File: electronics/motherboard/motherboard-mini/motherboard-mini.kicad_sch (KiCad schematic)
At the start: 76 parts, among them J1 TBP02R2-381-03BE, J2 TBP02R2-381-02BE, J3 ST1W008S4AR1500, J4 TBP02R2-381-03BE, J5 USB4070-30-C_REVC5, J6 CONUFL001-SMD-T, J7 21992304, J8 Conn_01x04_Male, J9 TBP02R2-381-02BE, Q1 BSS214NW, Q2 AOD417, U1 MCP73832-2-OT, U2 NCP718xSN500, U3 INA219BxD, U4 LT3652IMSE, U6 INA219BxD, U7 LD39015M33R, U8 MIC2145BMM, U9 RFM95W-915S2

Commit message: realign with master branch before kangaroo board is split into seperate repo
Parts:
- removed BT1: 1043, 1043:BAT_1043, symbol 1043:1043
- removed C12, C15: 1uF, Capacitor_SMD:C_0805_2012Metric, symbol Device:C
- removed C13, C16, C18: 10uF, Capacitor_SMD:C_0805_2012Metric, symbol Device:C
- removed C14: 0.01uF, Capacitor_SMD:C_0805_2012Metric, symbol Device:C
- removed C17: 100pF, Capacitor_SMD:C_0805_2012Metric, symbol Device:C
- removed D4: LED, LED_SMD:LED_0805_2012Metric, symbol Device:LED
- removed D5, D6: SS34LW_RVG, SS34LW_RVG:SODFL3718X102N, symbol SS34LW_RVG:SS34LW_RVG
- removed D8: BB-2020BGR-TRB, BB-2020BGR-TRB:LED_BB-2020BGR-TRB, symbol BB-2020BGR-TRB:BB-2020BGR-TRB
- removed D9: D_Schottky, SM5817PL:SODFL3718X108N, symbol Device:D_Schottky
- removed J1, J4: TBP02R2-381-03BE, TBP02R2-381-03BE:CUI_TBP02R2-381-03BE, symbol TBP02R2-381-03BE:TBP02R2-381-03BE
- removed J2, J9: TBP02R2-381-02BE, TBP02R2-381-02BE:CUI_TBP02R2-381-02BE, symbol TBP02R2-381-02BE:TBP02R2-381-02BE
- removed J3: ST1W008S4AR1500, ST1W008S4AR1500:JAE_ST1W008S4AR1500, symbol ST1W008S4AR1500:ST1W008S4AR1500
- removed J6: CONUFL001-SMD-T, CONUFL001-SMD-T:LINX_CONUFL001-SMD-T, symbol CONUFL001-SMD-T:CONUFL001-SMD-T
- removed J7: 21992304, 21992304:TE_21992304, symbol 21992304:21992304
- removed J8: Conn_01x04_Male, Connector_PinHeader_2.54mm:PinHeader_1x04_P2.54mm_Vertical, symbol Connector:Conn_01x04_Male
- removed L1: SRP4020T-5R6M, SRP4020TA-5R6M:IND_SRP4020TA-5R6M, symbol pspice:INDUCTOR
- removed L2: CBC2518T100M, CBC2518T100M:INDC2518X200N, symbol CBC2518T100M:CBC2518T100M
- removed MP1: 9774025151R, 9774025151R:WE_9774025151R, symbol 9774025151R:9774025151R
- removed Q1: BSS214NW, Package_TO_SOT_SMD:SOT-323_SC-70, symbol Transistor_FET:BSS214NW
- removed Q2: AOD417, AOD417:DPAK228P994X240_3N, symbol AOD417:AOD417
- removed R19: 91K, Resistor_SMD:R_0805_2012Metric, symbol Device:R
- removed R20: 330K, Resistor_SMD:R_0805_2012Metric, symbol Device:R
- removed R21: 0.1, Resistor_SMD:R_2512_6332Metric, symbol Device:R
- removed R22: 4.7K, Resistor_SMD:R_0805_2012Metric, symbol Device:R
- removed R28, R31: 100K, Resistor_SMD:R_0805_2012Metric, symbol Device:R
- removed R29: 1M, Resistor_SMD:R_0805_2012Metric, symbol Device:R
- removed R30, R33: 10K, Resistor_SMD:R_0805_2012Metric, symbol Device:R
- removed R34: 1K, Resistor_SMD:R_0805_2012Metric, symbol Device:R
- removed S1: DS04-254-2-02BK-SMT, DS04-254-2-02BK-SMT:SW_DS04-254-2-02BK-SMT, symbol DS04-254-2-02BK-SMT:DS04-254-2-02BK-SMT
- removed S2: RST, PTS636_SM43J_SMTR_LFS:SW_PTS636_SM43J_SMTR_LFS, symbol PTS636_SM43J_SMTR_LFS:PTS636_SM43J_SMTR_LFS
- removed S3: BOOT, PTS636_SM43J_SMTR_LFS:SW_PTS636_SM43J_SMTR_LFS, symbol PTS636_SM43J_SMTR_LFS:PTS636_SM43J_SMTR_LFS
- removed U1: MCP73832-2-OT, Package_TO_SOT_SMD:SOT-23-5, symbol Battery_Management:MCP73832-2-OT
- removed U2: NCP718xSN500, Package_TO_SOT_SMD:SOT-23-5, symbol Regulator_Linear:NCP718xSN500
- removed U3, U6: INA219BxD, Package_SO:SOIC-8_3.9x4.9mm_P1.27mm, symbol Analog_ADC:INA219BxD
- removed U4: LT3652IMSE, Package_SO:MSOP-12-1EP_3x4mm_P0.65mm_EP1.65x2.85mm, symbol Battery_Management:LT3652IMSE
- removed U7: LD39015M33R, Package_TO_SOT_SMD:SOT-23-5, symbol Regulator_Linear:LD39015M33R
- removed U8: MIC2145BMM, MIC2145BMM:MIC2145BMM, symbol MIC2145BMM:MIC2145BMM
- removed U9: RFM95W-915S2, RFM95W-915S2:XCVR_RFM95W-915S2, symbol RF_Module:RFM95W-915S2
- added C10: 22uF, Capacitor_SMD:C_0805_2012Metric, symbol Device:C
- added C7: 0.1uF, Capacitor_SMD:C_0805_2012Metric, symbol Device:C
- added C8: 12pF, Capacitor_SMD:C_0805_2012Metric, symbol Device:C
- added J1: JTAG, Connector_PinHeader_2.54mm:PinHeader_1x04_P2.54mm_Vertical, symbol Connector_Generic:Conn_01x04
- added J12: JTAG, 3221-10-0100-00:CNC_3221-10-0100-00, symbol Connector:Conn_ARM_JTAG_SWD_10
- added LS1: PS1240P02BT, PS1240P02BT:XDCR_PS1240P02BT, symbol PS1240P02BT:PS1240P02BT
- added Q1: MMDT3904, Package_TO_SOT_SMD:SOT-363_SC-70-6, symbol Transistor_BJT:MMDT3904
- added Q2: BC847, Package_TO_SOT_SMD:SOT-23, symbol Transistor_BJT:BC847
- added SW1: BOOT, 1977223-6:1977223-6, symbol 2022-10-04_00-56-22:1977223-6
- added SW2: RESET, 1977223-6:1977223-6, symbol 2022-10-04_00-56-22:1977223-6
- added SW3: PROG_BTN, 1977223-6:1977223-6, symbol 2022-10-04_00-56-22:1977223-6
- added U1: CP2102N-Axx-xQFN28, Package_DFN_QFN:QFN-28-1EP_5x5mm_P0.5mm_EP3.35x3.35mm, symbol Interface_USB:CP2102N-Axx-xQFN28
- added U2: ESP32-WROOM-32E_(16MB), ESP32-WROOM-32E__16MB_:XCVR_ESP32-WROOM-32E_(16MB), symbol ESP32-WROOM-32E__16MB_:ESP32-WROOM-32E_(16MB)
- added Y1: 32.768KHz, ABS07AIG-32:XTAL320X150X90, symbol ABS07AIG-32.768KHZ-T:ABS07AIG-32.768KHZ-T
- C1, C4: value 1uF -> 4.7uF
- C2: value 4.7uF -> 0.1uF
- C3: value 10uF -> 0.1uF
- C5: value 4.7uF -> 1uF
- C6: value 1uF -> 0.1uF
- C9: value 10uF -> 12pF
- D1: value LED(Red) -> LED(Orange)
- D2: value LED(Green) -> LED(Yellow)
- D3: value LED(Red) -> LED(Yellow)
- J5: footprint GCT_USB4070-30-C_REVC5 -> USB4145-03-0230-C_REVA:GCT_USB4145-03-0230-C_REVA
- R1: value 10K -> 1K
- R10: value 27K -> 10M
- R12: value 53.6K -> 10K
- R13: value 4.7K -> 1K
- R15: value 680 -> 4.7K
- R17, R2, R6: value 4.7K -> 10K
- R18: value 180K -> 2K
- R4: value 3.2K -> 1K
- R5: value 0.1 -> 1K; footprint Resistor_SMD:R_2512_6332Metric -> Resistor_SMD:R_0805_2012Metric
- R7, R8: value 4.7K -> 0
- R9: value 23K -> 10K
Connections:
- net +12V is gone; now on net GND: C1.1
- net D1 is gone; now on net +3.3V: R6.1
- net I2C_SDA1 is gone; now on net I2C_SCL: R16.2
- net +3.3V: now also C3.2, C4.2, R1.1, R12.1, R15.1, R4.1, R5.2, C10.2, C7.2, J1.1 (Pin_1), J12.1 (VTref), LS1.2, SW3.3, U1.6 (VDD), U2.2 (3V3); no longer R17.1, R3.1, R6.2
- net GND: now also C2.1, C3.1, C4.1, C5.1, C6.2, D3.1 (K), R17.2, C10.1, C7.1, C8.2, J1.4 (Pin_4), J12.3 (GND), J12.5 (GND), J12.9 (GNDDetect), Q2.2 (E), SW1.3, SW2.3, U1.29 (GND), U1.3 (GND), U2.1 (GND), U2.15 (GND), U2.38 (GND), U2.39_1 (GND), U2.39_2 (GND), U2.39_3 (GND), U2.39_4 (GND), U2.39_5 (GND), U2.39_6 (GND), U2.39_7 (GND), U2.39_8 (GND), U2.39_9 (GND); no longer C1.2, C2.2, C3.2, C4.2, C5.2, R10.2, R2.2, R4.1
- net GPIO0: now also Q1.3 (C2), SW1.1, U2.25 (IO0)
- net GPIO2: now also U2.24 (IO2)
- net GPIO4: now also U2.26 (IO4)
- net I2C_SCL: now also U2.37 (IO23)
- net I2C_SDA: now also R15.2, U2.10 (IO25); no longer R17.2
- net SPI_MISO: now also U2.31 (IO19)
- net SPI_MOSI: now also U2.30 (IO18)
- net SPI_SCK: now also U2.29 (IO5)
- net USB_D+: now also U1.4 (D+)
- net USB_D-: now also U1.5 (D-)
- net VBUS: now also C1.2, C2.2, U1.8 (VBUS); no longer C2.1
- net at D1.2 (A): now also R4.2; no longer R2.1
- net GPIO17: now reaches R9.1
- net GPIO17: now also U2.28 (IO17)
- net ESP_ENABLE: now reaches C6.1
- net ESP_ENABLE: now also C5.2, R6.2, Q1.6 (C1), SW2.1, U2.3 (EN)
- net at D1.1 (K): now also U1.19 (~{TXT}/GPIO.0)
- net at D3.2 (A): now also R18.2; no longer R8.2
- net at R1.2: now also U1.9 (~{RST})
- net at D2.2 (A): now also R5.1; no longer R7.2
- net GPIO13: now reaches R18.1
- net GPIO13: now also J12.4 (SWDCLK/TCK), U2.16 (IO13)
- net at D2.1 (K): now also U1.18 (~{RXT}/GPIO.1)
- removed net +5VP: C4.1, R1.1
- net D0 renamed UART_RTS
- net UART_RTS: now also Q1.1 (E1), U1.24 (~{RTS})
- net I2C_SCL1: no longer names the net of R13.2
- net I2C_SCL1: now also LS1.1, Q2.3 (C)
- net VBAT: no longer names the net of C9.1
- net VBAT: now also R10.2, R7.1, Y1.2; no longer C5.1
- new net: R7.2, U2.8 (IO32)
- new net: R12.2, U2.27 (IO16)
- new net: Q2.1 (B), R9.2
- new net: Q1.5 (B2), R3.1
- new net: C8.1, R10.1, R8.1, Y1.1
- new net: R8.2, U2.9 (IO33)
- new net: Q1.2 (B1), R2.1
- new net: U2.17 (NC), U2.18 (NC), U2.19 (NC), U2.20 (NC), U2.21 (NC), U2.22 (NC)
- new net A2: U2.6 (IO34)
- new net GPIO12: J12.8 (NC/TDI), U2.14 (IO12)
- new net GPIO14: J12.2 (SWDIO/TMS), U2.13 (IO14)
- new net GPIO15: J12.6 (SWO/TDO), U2.23 (IO15)
- new net GPIO21: U2.33 (IO21)
- new net GPIO27: U2.12 (IO27)
- new net GPIO36: U2.4 (SENSOR_VP)
- new net GPIO39: U2.5 (SENSOR_VN)
- new net IO_P2: R17.1, SW3.1
- new net UART_DTR: Q1.4 (E2), R2.2, U1.28 (~{DTR})
- new net UART_RX0: J1.2 (Pin_2), U1.26 (TXD), U2.34 (RXD0)
- new net UART_RX1: U2.11 (IO26)
- new net UART_TX0: J1.3 (Pin_3), U1.25 (RXD), U2.35 (TXD0)
- new net UART_TX1: U2.36 (IO22)
- no-connect marks 30 -> 38
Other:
- added sheet cat_m1 (cat_m1.kicad_sch)
- added sheet peripherals (peripherals.kicad_sch)
- added sheet power_distribution (power_distribution.kicad_sch)
- note added: "Annemometer Dir"
- note added: "Annemometer Spd"
- note added: "Auto-Reset"
- note added: "Buttons"
- note added: "CAT-M1"
- note added: "Debug(TDI)"
- note added: "Debug(TDO)"
- note added: "Debug(TMS)"
- note added: "ESP32-WROOM-32E-N16"
- note added: "ESR=70Kohm"
- note added: "Indicator LED/Debug(TCK)"
- note added: "One-Wire"
- note added: "Peripherals"
- note added: "Piezo Buzzer"
- note added: "Piezo Buzzer Control"
- note added: "Power Distribution"
- note added: "SDI-12"
- note added: "UART Interface"
- note added: "USB-to-UART Interface"
- note removed: "10uH"
- note removed: "12V Solar"
- note removed: "12V Step-Up Converter"
- note removed: "150mA"
- note removed: "1W (2512)"
- note removed: "3.3V Low-dropout Regulator"
- note removed: "50 uA (Quiescent) 0.1V @ 100mA (Drop-out)"
- note removed: "5V (200 mA) Li-Ion USB Battery Charger"
- note removed: "5V LDO"
- note removed: "5V Solar"
- note removed: "Battery V & I Monitoring I2C = 0x45"
- note removed: "Charging"
- note removed: "Connector to RR11122FWC switch"
- note removed: "Fault"
- note removed: "I(Reg) = 1000/R(Prog)"
- note removed: "LED Indicators"
- note removed: "LoRaWAN Interface (Requires external antenna)"
- note removed: "One-Wire Interface"
- note removed: "Put 12V(EN) high to enable a 12 V output"
- note removed: "R1"
- note removed: "R2"
- note removed: "Reverse Polarity Protection"
- note removed: "SD-Card Interface"
- note removed: "SDI-12 Interface"
- note removed: "SM5817PL"
- note removed: "SWD Debug Interface"
- note removed: "Single Cell Li-Ion 18650 (4.2 V)"
- note removed: "Solar Charger (12V or 5V Panels)"
- note removed: "Solar V & I Monitoring I2C = 0x40"
- note removed: "V(out) = 12.0 V R2 = (1.08 x R1) / (V(out) - 1.08)"
- note removed: "~250 mA"
- moved on the sheet: J5, R11, R14

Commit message: added mounting circuit board and updated motherboard for next itteration
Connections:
- net A2 is gone; now on net GPIO34: U2.6 (IO34)
- net +3.3V: now also SW3.4; no longer SW3.3
- net ESP_ENABLE: now also SW2.2; no longer SW2.1
- net GND: now also SW2.4; no longer SW2.3
- net UART_RX0: now also U2.35 (TXD0); no longer U2.34 (RXD0)
- net UART_TX0: now also U2.34 (RXD0); no longer U2.35 (TXD0)
- net GPIO34: now reaches SW3.2
- net GPIO34: now also R17.1
- net GPIO2: no longer names the net of U2.24 (IO2)
- net GPIO21: no longer names the net of U2.33 (IO21)
- net GPIO27: no longer names the net of U2.12 (IO27)
- net GPIO39: no longer names the net of U2.5 (SENSOR_VN)
- net GPIO4: no longer names the net of U2.26 (IO4)
- net IO_P2: no longer names the net of SW3.1
- net IO_P2: no longer R17.1
- no-connect marks 38 -> 43
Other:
- note added: "Pull-down resistors on CC1 and CC2 required as part of the USB-C spec. to identify a device has been connected and power should be applied"
- note removed: "Annemometer Dir"
- note removed: "Annemometer Spd"
- note removed: "One-Wire"
- moved on the sheet: C6, R17, SW3

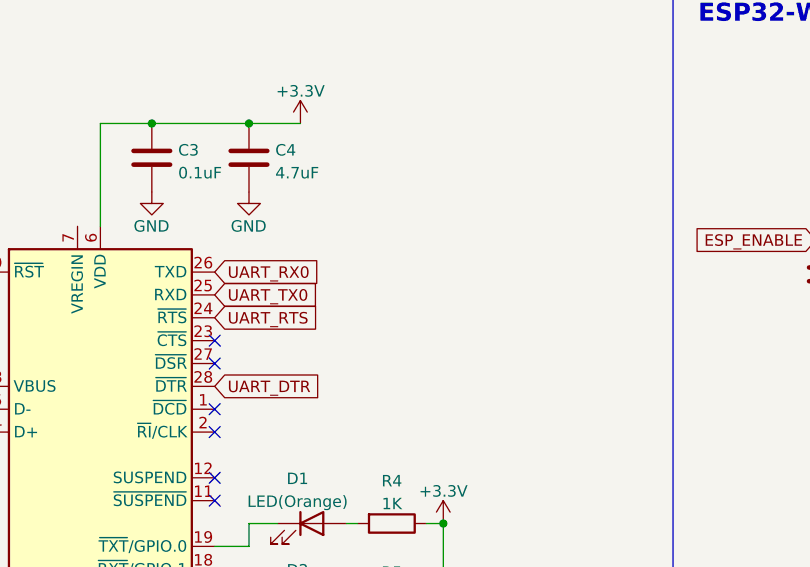
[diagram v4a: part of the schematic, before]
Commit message: added ble uart bidirectional tests
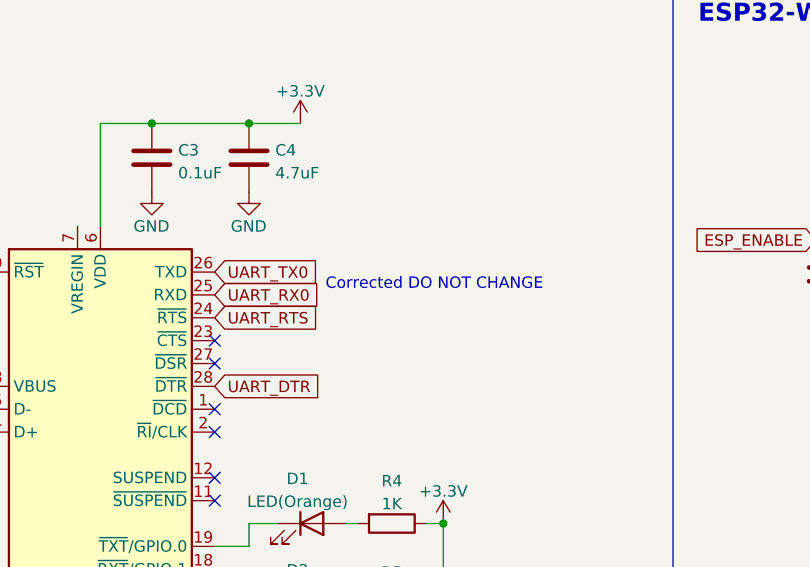
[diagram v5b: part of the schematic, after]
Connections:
- net UART_RX0: now also U1.25 (RXD); no longer U1.26 (TXD)
- net UART_TX0: now also U1.26 (TXD); no longer U1.25 (RXD)
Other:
- note added: "Corrected DO NOT CHANGE"
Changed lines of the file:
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@@
+    (effects (font (size 1.27 1.27)) (justify left bottom))
+  )
+  (text "Corrected DO NOT CHANGE" (at 93.218 130.175 0)
     (effects (font (size 1.27 1.27)) (justify left bottom))
   )
@@
     )
   )
-  (global_label "UART_RX0" (shape input) (at 80.899 128.016 0) (fields_autoplaced)
+  (global_label "UART_RX0" (shape input) (at 80.899 130.556 0) (fields_autoplaced)
     (effects (font (size 1.27 1.27)) (justify left))
-    (property "Intersheet References" "${INTERSHEET_REFS}" (id 0) (at 92.6254 127.9366 0)
+    (property "Intersheet References" "${INTERSHEET_REFS}" (id 0) (at 92.6254 130.4766 0)
       (effects (font (size 1.27 1.27)) (justify left) hide)
     )
@@
     )
   )
-  (global_label "UART_TX0" (shape input) (at 80.899 130.556 0) (fields_autoplaced)
+  (global_label "UART_TX0" (shape input) (at 80.899 128.016 0) (fields_autoplaced)
     (effects (font (size 1.27 1.27)) (justify left))
-    (property "Intersheet References" "${INTERSHEET_REFS}" (id 0) (at 92.3231 130.4766 0)
+    (property "Intersheet References" "${INTERSHEET_REFS}" (id 0) (at 92.3231 127.9366 0)
       (effects (font (size 1.27 1.27)) (justify left) hide)
     )
@@
       (reference "#PWR094") (unit 1) (value "GND") (footprint "")
     )
-    (path "/b973fe11-f1e1-4488-b69d-471e9c144d9a/6fcbe775-786e-484b-bb9c-17e850ecf273"
-      (reference "#PWR095") (unit 1) (value "GND") (footprint "")
-    )
     (path "/b973fe11-f1e1-4488-b69d-471e9c144d9a/9f2edb33-15c4-4786-b0cf-525ab0fcb4b0"
       (reference "#PWR096") (unit 1) (value "VCC") (footprint "")
@@
       (reference "#PWR097") (unit 1) (value "GND") (footprint "")
     )
-    (path "/b973fe11-f1e1-4488-b69d-471e9c144d9a/ec1a91e1-e600-4c08-83c8-59252875c41d"
-      (reference "#PWR098") (unit 1) (value "GND") (footprint "")
-    )
     (path "/b973fe11-f1e1-4488-b69d-471e9c144d9a/43b029a2-9759-4a70-abde-7178f05aaf11"
       (reference "#PWR099") (unit 1) (value "GND") (footprint "")
@@
       (reference "#PWR0135") (unit 1) (value "GND") (footprint "")
     )
+    (path "/b973fe11-f1e1-4488-b69d-471e9c144d9a/0be08d22-dd14-46f0-ace7-73ddbf8baab5"
+      (reference "#PWR?") (unit 1) (value "GND") (footprint "")
+    )
+    (path "/b973fe11-f1e1-4488-b69d-471e9c144d9a/44b1ec5a-270c-4427-a94d-a36548955c20"
+      (reference "#PWR?") (unit 1) (value "GND") (footprint "")
+    )
+    (path "/b973fe11-f1e1-4488-b69d-471e9c144d9a/55b32408-644e-48ab-a1f8-b6b06120e05e"
+      (reference "#PWR?") (unit 1) (value "GND") (footprint "")
+    )
+    (path "/b973fe11-f1e1-4488-b69d-471e9c144d9a/65d7e112-df57-489f-98e4-9452c277988b"
+      (reference "#PWR?") (unit 1) (value "GND") (footprint "")
+    )
     (path "/81efa281-7ef6-4b2c-aac2-b705d10ab725/882b778f-a755-40ef-a049-a1b2ba7bd935"
       (reference "BT1") (unit 1) (value "1043") (footprint "1043:BAT_1043")
@@
       (reference "C35") (unit 1) (value "0.1uF") (footprint "Capacitor_SMD:C_0805_2012Metric")
     )
+    (path "/b973fe11-f1e1-4488-b69d-471e9c144d9a/1fc0d8b2-2ead-42fd-8f66-a45924997420"
+      (reference "CR?") (unit 1) (value "PESD0402-140") (footprint "PESD0402")
+    )
+    (path "/b973fe11-f1e1-4488-b69d-471e9c144d9a/2ce3d97c-6ff2-40ce-9861-7a9bc59a71ae"
+      (reference "CR?") (unit 1) (value "PESD0402-140") (footprint "PESD0402")
+    )
+    (path "/b973fe11-f1e1-4488-b69d-471e9c144d9a/32694522-30fd-45d1-a248-e6a9a92d14e3"
+      (reference "CR?") (unit 1) (value "PESD0402-140") (footprint "PESD0402")
+    )
+    (path "/b973fe11-f1e1-4488-b69d-471e9c144d9a/8ddd4fd4-9c59-456a-b108-429396bed21f"
+      (reference "CR?") (unit 1) (value "PESD0402-140") (footprint "PESD0402")
+    )
     (path "/45636123-592d-4564-8885-623efe02ff34"
       (reference "D1") (unit 1) (value "LED(Orange)") (footprint "LED_SMD:LED_0805_2012Metric")
@@
       (reference "U11") (unit 1) (value "SARA-R410M-02B") (footprint "SARA-R410M-02B:XCVR_SARA-R410M-02B")
     )
-    (path "/b973fe11-f1e1-4488-b69d-471e9c144d9a/690e15bd-40f1-4163-9c6f-c6645cba2c73"
-      (reference "U12") (unit 1) (value "AOZ8904CIL") (footprint "AOZ8904CIL:AOZ8904CIL")
-    )
     (path "/b973fe11-f1e1-4488-b69d-471e9c144d9a/51adc328-a3c7-49c2-aecb-0a7f82e0175e"

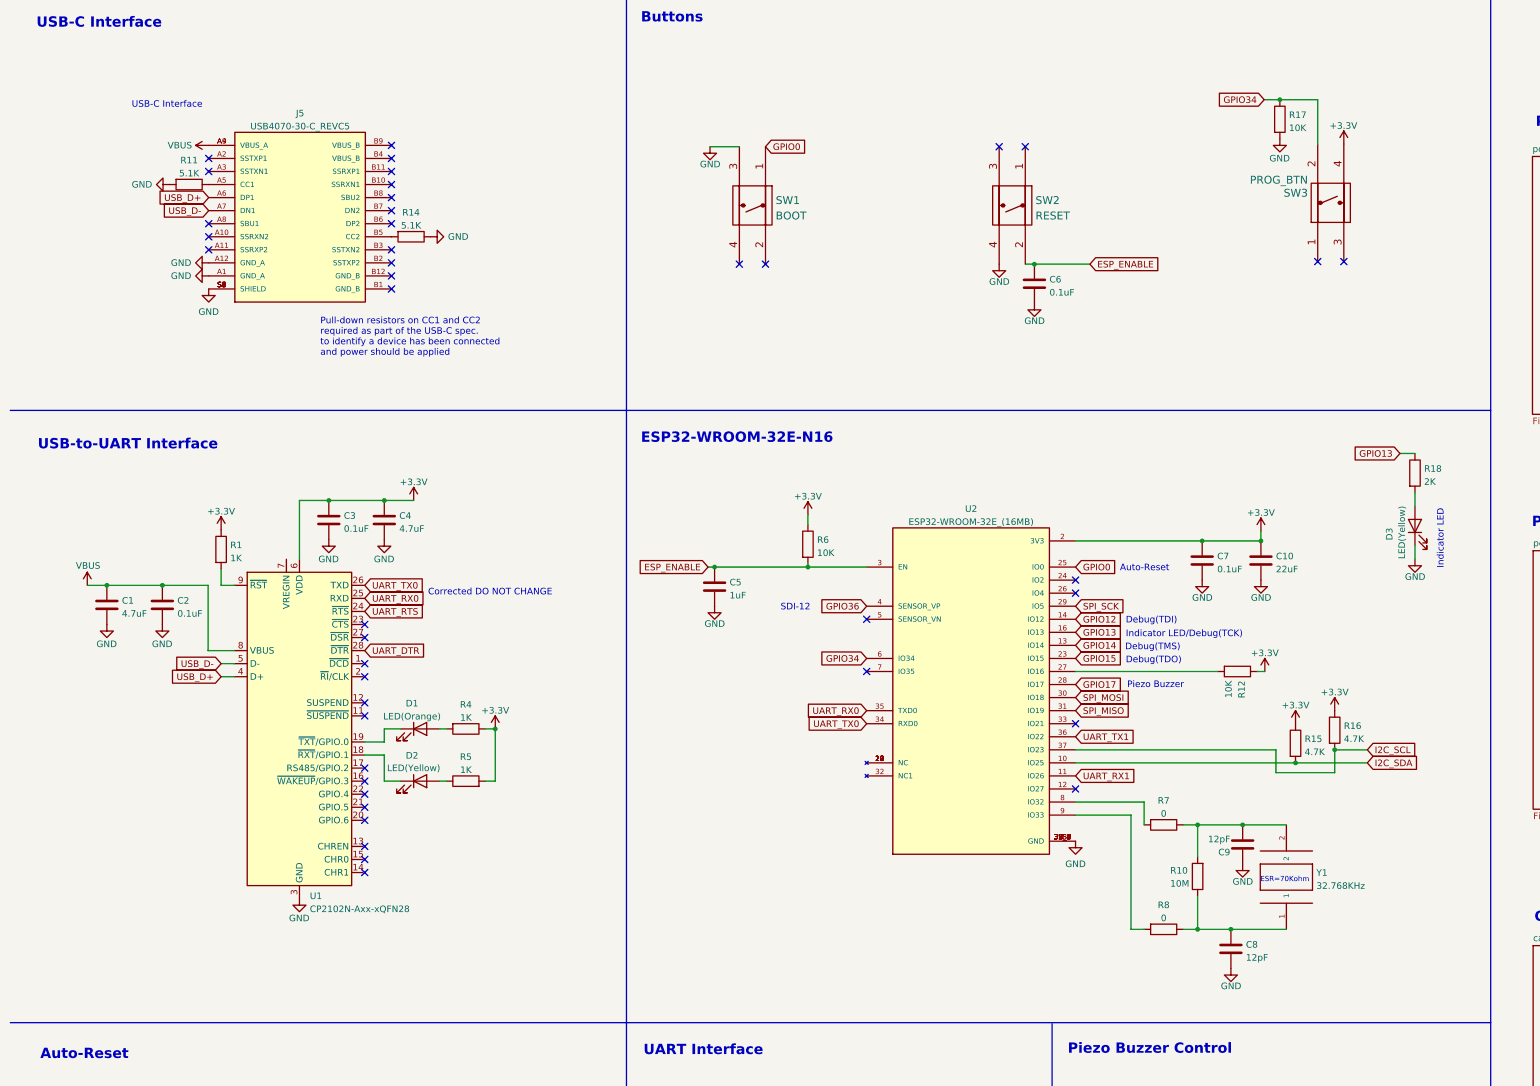
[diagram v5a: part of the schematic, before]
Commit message: new board version sent for production, termed 'wombat' and breakout board
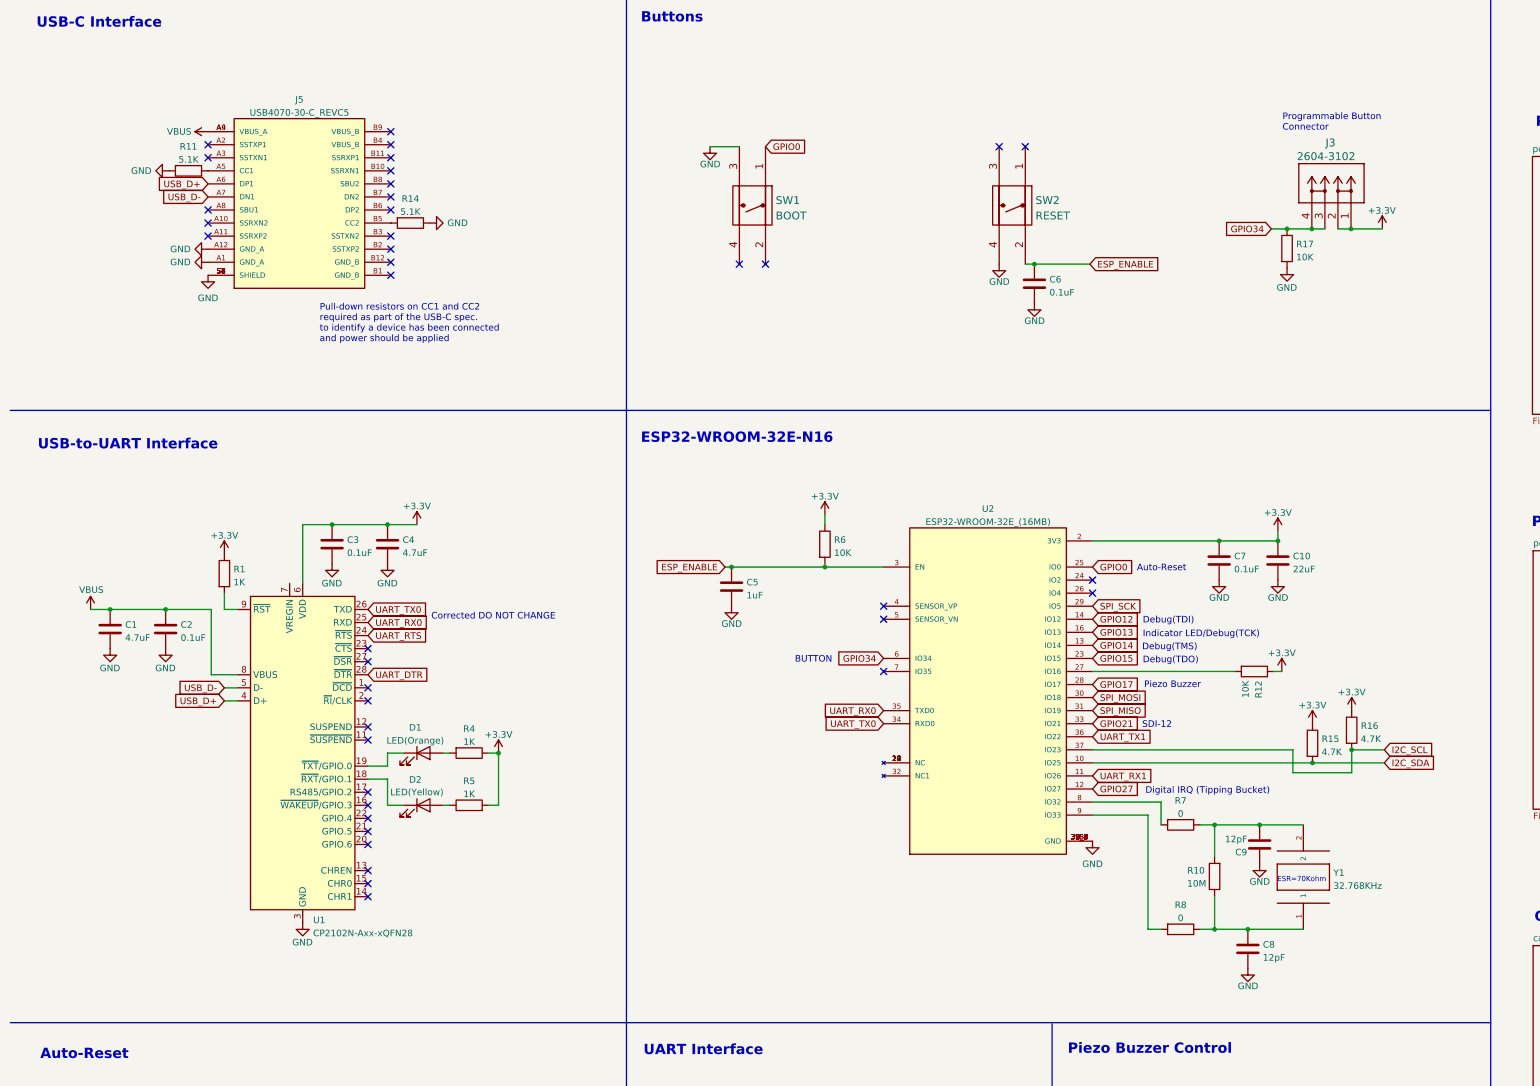
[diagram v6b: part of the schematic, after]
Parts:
- removed D3: LED(Yellow), LED_SMD:LED_0805_2012Metric, symbol Device:LED
- removed R18: 2K, Resistor_SMD:R_0805_2012Metric, symbol Device:R
- removed SW3: PROG_BTN, 1977223-6:1977223-6, symbol 2022-10-04_00-56-22:1977223-6
- added J3: 2604-3102, 2604-3102:2604-3102, symbol 2604-3102:2604-3102
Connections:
- net +3.3V: now also J3.1, J3.2
- net GPIO34: now also J3.3, J3.4
- net GPIO27: now reaches U2.12 (IO27)
- net GPIO21: now reaches U2.33 (IO21)
- net GPIO36: no longer names the net of U2.4 (SENSOR_VP)
- no-connect marks 43 -> 40
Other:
- note added: "BUTTON"
- note added: "Digital IRQ (Tipping Bucket)"
- note added: "Programmable Button Connector"
- note removed: "Indicator LED"
- moved on the sheet: C1, C10, C2, C3, C4, C5, C7, C8, C9, D1, D2, J5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
